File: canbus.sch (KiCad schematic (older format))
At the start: 17 parts, among them U5 MCP2515-xST, U6 ISO1050DUB, U7 H7550-H#, Y1 1C208000BC0R

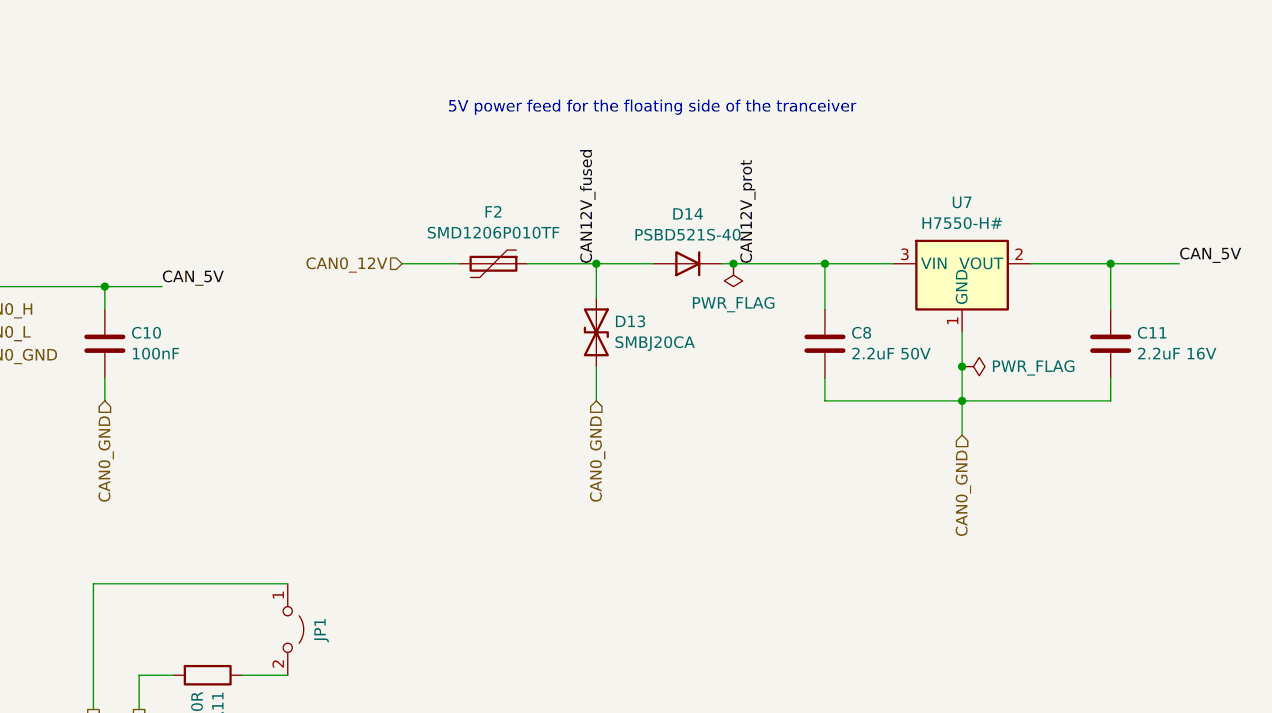
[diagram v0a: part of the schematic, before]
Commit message: Revert back to using INA199 as a current limiter
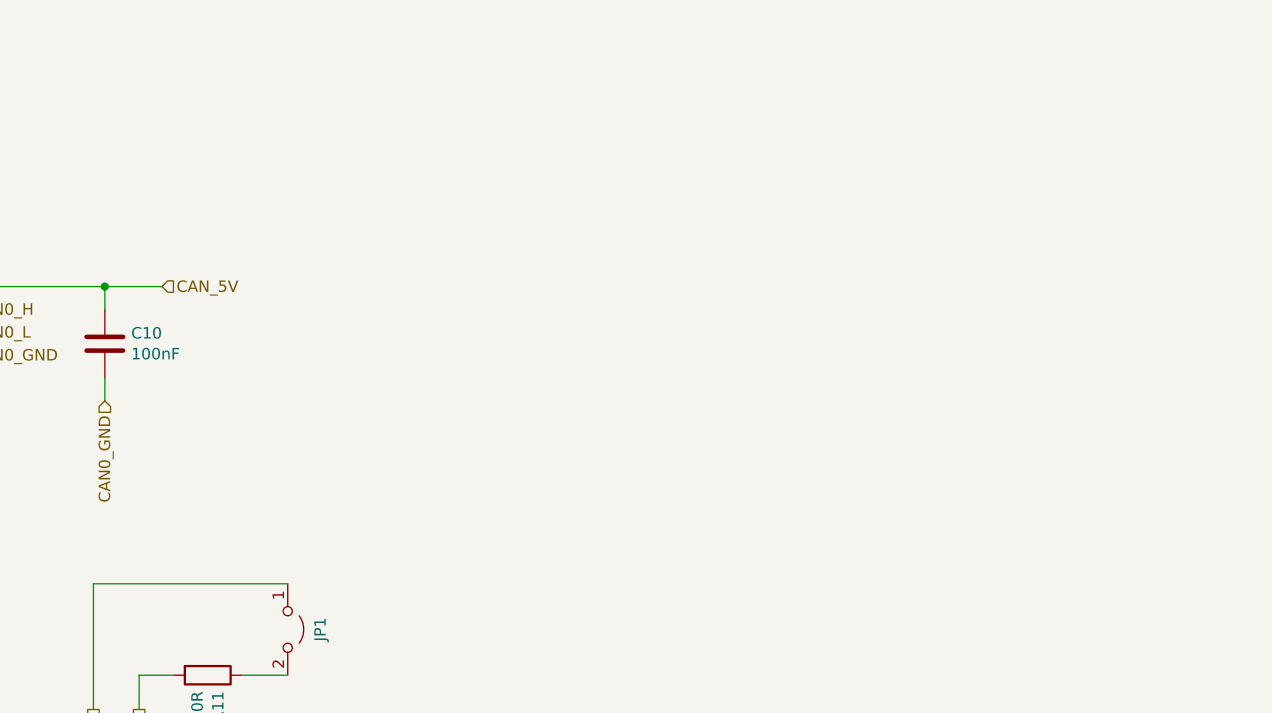
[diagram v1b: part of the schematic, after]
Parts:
- removed C11: 2.2uF 16V, Capacitor_SMD:C_0603_1608Metric, symbol Device:C
- removed C8: 2.2uF 50V, Capacitor_SMD:C_1206_3216Metric, symbol Device:C
- removed D13: SMBJ20CA, Diode_SMD:D_SMB, symbol Device:D_TVS
- removed D14: PSBD521S-40, Diode_SMD:D_SOD-523, symbol Device:D
- removed F2: SMD1206P010TF, Fuse:Fuse_1206_3216Metric, symbol Device:Polyfuse
- removed U7: H7550-H#, Package_TO_SOT_SMD:SOT-23, symbol sailor-hat:HT75xx-1-SOT23
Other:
- note removed: "5V power feed for the floating side of the tranceiver"
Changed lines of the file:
@@
 Text HLabel 3350 2350 2    50   Output ~ 0
 INT0
-$Comp
-L sailor-hat:HT75xx-1-SOT23 U7
-U 1 1 5F3E4347
-P 9500 1650
-F 0 "U7" H 9500 2017 50  0000 C CNN
-F 1 "H7550-H#" H 9500 1926 50  0000 C CNN
-F 2 "Package_TO_SOT_SMD:SOT-23" H 9500 1975 50  0001 C CIN
-F 3 "" H 9500 1750 50  0001 C CNN
-F 4 "C277875" H 9500 1650 50  0001 C CNN "LCSC"
-	1    9500 1650
-	1    0    0    -1
-$EndComp
-$Comp
-L Device:Polyfuse F2
-U 1 1 5F3E5EE7
-P 7450 1550
-F 0 "F2" V 7225 1550 50  0000 C CNN
-F 1 "SMD1206P010TF" V 7316 1550 50  0000 C CNN
-F 2 "Fuse:Fuse_1206_3216Metric" H 7500 1350 50  0001 L CNN
-F 3 "~" H 7450 1550 50  0001 C CNN
-F 4 "C20981" H 7450 1550 50  0001 C CNN "LCSC"
-	1    7450 1550
-	0    1    1    0
-$EndComp
-$Comp
-L Device:D_TVS D13
-U 1 1 5F3E659B
-P 7900 1850
-F 0 "D13" V 7854 1929 50  0000 L CNN
-F 1 "SMBJ20CA" V 7945 1929 50  0000 L CNN
-F 2 "Diode_SMD:D_SMB" H 7900 1850 50  0001 C CNN
-F 3 "~" H 7900 1850 50  0001 C CNN
-F 4 "C113992" H 7900 1850 50  0001 C CNN "LCSC"
-	1    7900 1850
-	0    1    1    0
-$EndComp
-$Comp
-L Device:D D14
-U 1 1 5F3F180C
-P 8300 1550
-F 0 "D14" H 8300 1334 50  0000 C CNN
-F 1 "PSBD521S-40" H 8300 1425 50  0000 C CNN
-F 2 "Diode_SMD:D_SOD-523" H 8300 1550 50  0001 C CNN
-F 3 "~" H 8300 1550 50  0001 C CNN
-F 4 "C168633" H 8300 1550 50  0001 C CNN "LCSC"
-	1    8300 1550
-	-1   0    0    1
-$EndComp
-Wire Wire Line
-	7600 1550 7900 1550
-Wire Wire Line
-	8450 1550 8500 1550
-Wire Wire Line
-	9500 2300 9500 2150
-Wire Wire Line
-	7900 1700 7900 1550
-Connection ~ 7900 1550
-Wire Wire Line
-	7900 1550 8150 1550
-Wire Wire Line
-	7900 2000 7900 2150
-Text Label 10450 1550 0    50   ~ 0
-CAN_5V
-Text Label 6000 1650 0    50   ~ 0
-CAN_5V
 Wire Wire Line
 	4100 1650 4300 1650
@@
 Text HLabel 5100 1850 2    50   Input ~ 0
 CAN0_L
-Text HLabel 7050 1550 0    50   Input ~ 0
-CAN0_12V
-Text HLabel 7900 2150 3    50   Input ~ 0
-CAN0_GND
 Text HLabel 5100 1950 2    50   Input ~ 0
-CAN0_GND
-Text HLabel 9500 2300 3    50   Input ~ 0
 CAN0_GND
 Wire Wire Line
@@
 Wire Wire Line
 	3350 1850 4300 1850
-Text Notes 7250 900  0    50   ~ 0
-5V power feed for the floating side of the tranceiver
-$Comp
-L power:PWR_FLAG #FLG0107
-U 1 1 5F4B09EE
-P 8500 1550
-F 0 "#FLG0107" H 8500 1625 50  0001 C CNN
-F 1 "PWR_FLAG" H 8500 1723 50  0000 C CNN
-F 2 "" H 8500 1550 50  0001 C CNN
-F 3 "~" H 8500 1550 50  0001 C CNN
-	1    8500 1550
-	-1   0    0    1
-$EndComp
-Connection ~ 8500 1550
-Wire Wire Line
-	8500 1550 8900 1550
-$Comp
-L power:PWR_FLAG #FLG0108
-U 1 1 5F4B190A
-P 9500 2000
-F 0 "#FLG0108" H 9500 2075 50  0001 C CNN
-F 1 "PWR_FLAG" V 9500 2128 50  0000 L CNN
-F 2 "" H 9500 2000 50  0001 C CNN
-F 3 "~" H 9500 2000 50  0001 C CNN
-	1    9500 2000
-	0    1    1    0
-$EndComp
-Connection ~ 9500 2000
-Wire Wire Line
-	9500 2000 9500 1850
 Text Label 3650 1750 0    50   ~ 0
 CAN_RX
@@
 Text Label 1800 2900 0    50   ~ 0
 OSC1
-Wire Wire Line
-	7050 1550 7300 1550
 $Comp
 L power:GND #PWR0117
@@
 Wire Wire Line
 	5750 1650 5100 1650
-Text Label 7900 1550 1    50   ~ 0
-CAN12V_fused
-Text Label 8600 1550 1    50   ~ 0
-CAN12V_prot
 Text HLabel 5750 2150 3    50   Input ~ 0
 CAN0_GND
-$Comp
-L Device:C C?
-U 1 1 5F3C81F3
-P 8900 1900
-AR Path="/5CA65CC5/5F3C81F3" Ref="C?"  Part="1"
-AR Path="/5C348474/5F3C81F3" Ref="C8"  Part="1"
-F 0 "C8" H 9015 1946 50  0000 L CNN
-F 1 "2.2uF 50V" H 9015 1855 50  0000 L CNN
-F 2 "Capacitor_SMD:C_1206_3216Metric" H 8938 1750 50  0001 C CNN
-F 3 "~" H 8900 1900 50  0001 C CNN
-F 4 "C50254" H 8900 1900 50  0001 C CNN "LCSC"
-	1    8900 1900
-	1    0    0    -1
-$EndComp
-$Comp
-L Device:C C?
-U 1 1 5F3C9CED
-P 10150 1900
-AR Path="/5CA65CC5/5F3C9CED" Ref="C?"  Part="1"
-AR Path="/5C348474/5F3C9CED" Ref="C11"  Part="1"
-F 0 "C11" H 10265 1946 50  0000 L CNN
-F 1 "2.2uF 16V" H 10265 1855 50  0000 L CNN
-F 2 "Capacitor_SMD:C_0603_1608Metric" H 10188 1750 50  0001 C CNN
-F 3 "~" H 10150 1900 50  0001 C CNN
-F 4 "C23630" H 10150 1900 50  0001 C CNN "LCSC"
-	1    10150 1900
-	1    0    0    -1
-$EndComp
-Wire Wire Line
-	8900 1750 8900 1550
-Connection ~ 8900 1550
-Wire Wire Line
-	8900 1550 9200 1550
-Wire Wire Line
-	10150 1750 10150 1550
-Wire Wire Line
-	10150 1550 9800 1550
-Wire Wire Line
-	10450 1550 10150 1550
-Connection ~ 10150 1550
-Wire Wire Line
-	8900 2050 8900 2150
-Wire Wire Line
-	8900 2150 9500 2150
-Connection ~ 9500 2150
-Wire Wire Line
-	9500 2150 9500 2000
-Wire Wire Line
-	9500 2150 10150 2150
-Wire Wire Line
-	10150 2150 10150 2050
+Text HLabel 6000 1650 2    50   Input ~ 0
+CAN_5V
 $EndSCHEMATC

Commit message: Update components according to JLCPCB availability
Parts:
- Y1: value 1C208000BC0R -> 1C208000CE0Q; LCSC C57131 -> C133366
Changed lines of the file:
@@
 P 1550 3250
 F 0 "Y1" H 1744 3296 50  0000 L CNN
-F 1 "1C208000BC0R" H 1744 3205 50  0000 L CNN
+F 1 "1C208000CE0Q" H 1744 3205 50  0000 L CNN
 F 2 "Crystal:Crystal_SMD_3225-4Pin_3.2x2.5mm" H 1550 3250 50  0001 C CNN
 F 3 "~" H 1550 3250 50  0001 C CNN
-F 4 "C57131" H 1550 3250 50  0001 C CNN "LCSC"
+F 4 "C133366" H 1550 3250 50  0001 C CNN "LCSC"
 	1    1550 3250
 	1    0    0    -1

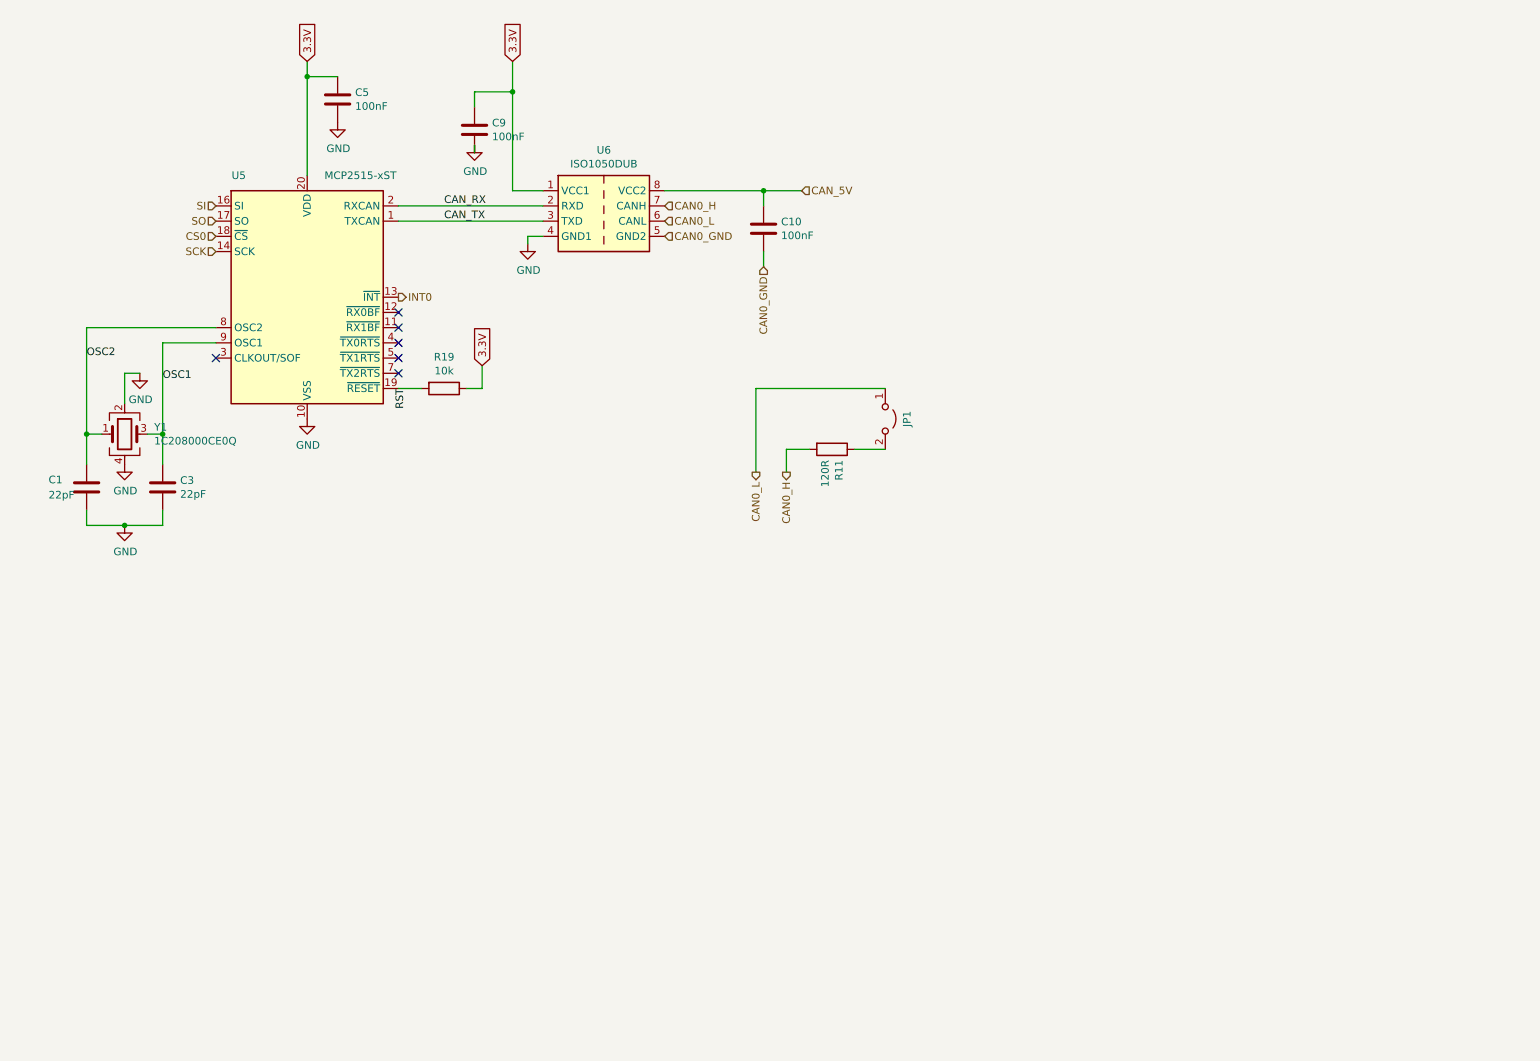
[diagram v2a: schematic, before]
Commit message: Schema updated
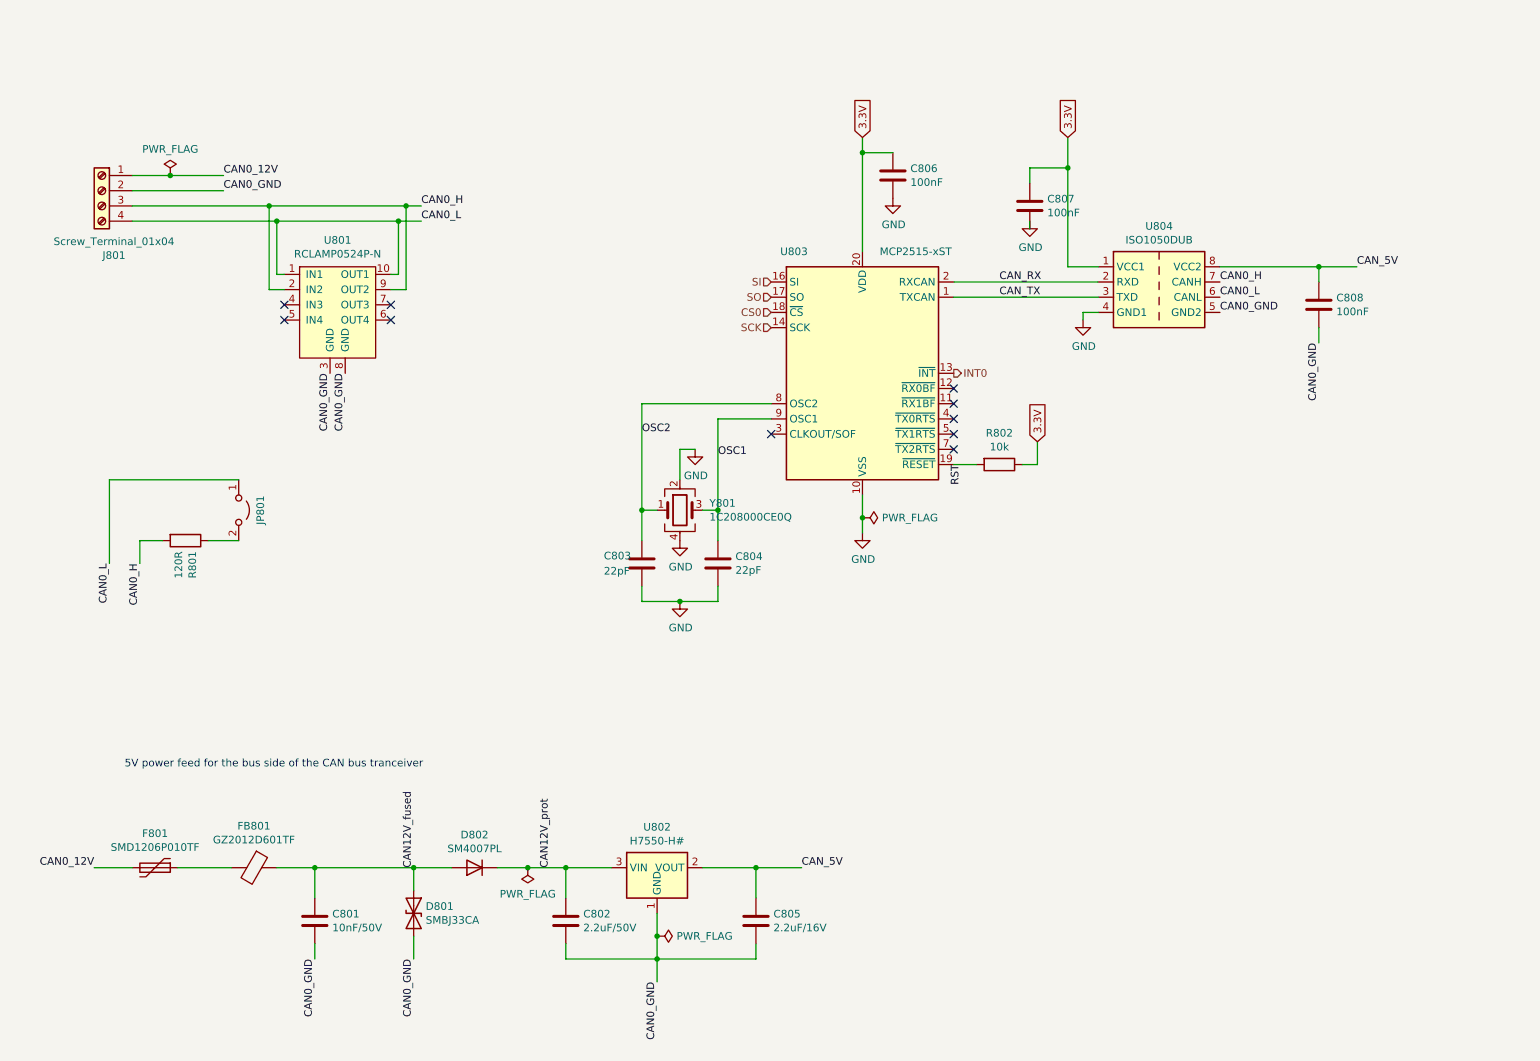
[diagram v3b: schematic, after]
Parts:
- added C801: 10nF/50V, Capacitor_SMD:C_0402_1005Metric, symbol Device:C
- added C802: 2.2uF/50V, Capacitor_SMD:C_1206_3216Metric, symbol Device:C
- added C805: 2.2uF/16V, Capacitor_SMD:C_0603_1608Metric, symbol Device:C
- added D801: SMBJ33CA, Diode_SMD:D_SMB, symbol Device:D_TVS
- added D802: SM4007PL, Diode_SMD:D_SOD-123F, symbol Device:D
- added F801: SMD1206P010TF, Fuse:Fuse_1206_3216Metric, symbol Device:Polyfuse
- added FB801: GZ2012D601TF, Inductor_SMD:L_0805_2012Metric, symbol Device:Ferrite_Bead
- added J801: Screw_Terminal_01x04, custom:TerminalBlock_WJ15EDGRC-3.81-4P, symbol Connector:Screw_Terminal_01x04
- added U801: RCLAMP0524P-N, symbol sailor-hat:RCLAMP0524P-N
- added U802: H7550-H#, Package_TO_SOT_SMD:SOT-23, symbol sailor-hat:HT75xx-1-SOT23
- renumbered C1 to C803, C3 to C804, C5 to C806, C9 to C807, C10 to C808, JP1 to JP801, R11 to R801, R19 to R802, U5 to U803, U6 to U804, Y1 to Y801
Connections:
- net CAN0_GND: now also C801.2, C802.2, C805.2, D801.2 (A2), J801.2 (Pin_2), U801.3 (GND), U801.8 (GND), U802.1 (GND)
- net CAN0_H: now also J801.3 (Pin_3), U801.2 (IN2), U801.9 (OUT2)
- net CAN0_L: now also J801.4 (Pin_4), U801.1 (IN1), U801.10 (OUT1)
- net CAN_5V: now also C805.1, U802.2 (VOUT)
- new net: F801.1, FB801.2
- new net CAN0_12V: F801.2, J801.1 (Pin_1)
- new net CAN12V_fused: C801.1, D801.1 (A1), D802.2 (A), FB801.1
- new net CAN12V_prot: C802.1, D802.1 (K), U802.3 (VIN)
- no-connect marks 6 -> 10
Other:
- note added: "5V power feed for the bus side of the CAN bus tranceiver"
- moved on the sheet: C803, C804, C806, C807, C808, JP801, R801, R802, U803, U804, Y801
